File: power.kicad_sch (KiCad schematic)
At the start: 28 parts, among them J3 Conn_01x02, Q2 AO3401A, SW8 SW_Slide_DPDT, U3 TP4056-42-ESOP8, U4 INA219AxDCN, U7 TPS62160DGK

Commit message: more switch, change to sideways leds, move battery connector
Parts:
- D1: value GREEN -> ORANGE; LCSC C22371297 -> C965861; Manufacturer HONGLITRONIC -> XINGLIGHT; Manufacturer Part Number PSC-1608U52GC-G4 -> XL-1606UOC
- D2: LCSC C2286 -> C965860; Manufacturer Hubei KENTO Elec -> XINGLIGHT; Manufacturer Part Number KT-0603R -> XL-1606SURC
- D5: LCSC C22371297 -> C965863; Manufacturer HONGLITRONIC -> XINGLIGHT; Manufacturer Part Number PSC-1608U52GC-G4 -> XL-1606UGC
- SW8: footprint Button_Switch_SMD:SW_DPDT_CK_JS202011JCQN -> Button_Switch_SMD:SW_SPDT_CK_JS102011SAQN; symbol Switch:SW_Slide_DPDT -> Switch:SW_SPDT; LCSC C221665 -> C221660; Manufacturer Part Number JS202011JCQN -> JS102011SAQN
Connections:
- net at SW8.1 (A): now also R35.1, U4.1 (IN+)
- net at SW8.2 (B): now also D3.1 (K), Q2.2 (S)
- no-connect marks 4 -> 1
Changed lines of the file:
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@@
 (kicad_sch
-	(version 20260101)
+	(version 20260306)
 	(generator "eeschema")
 	(generator_version "10.0")
@@
 	)
 	(no_connect
-		(at 154.94 104.14)
-	)
-	(no_connect
-		(at 165.1 93.98)
-	)
-	(no_connect
-		(at 160.02 104.14)
-	)
-	(no_connect
-		(at 165.1 104.14)
+		(at 160.02 92.71)
 	)
 	(wire
@@
 	(wire
 		(pts
-			(xy 154.94 90.17) (xy 154.94 93.98)
-		)
-		(stroke
-			(width 0)
-			(type default)
-		)
-	)
-	(wire
-		(pts
 			(xy 226.06 57.15) (xy 246.38 57.15)
 		)
@@
 	(wire
 		(pts
+			(xy 160.02 87.63) (xy 160.02 40.64)
+		)
+		(stroke
+			(width 0)
+			(type default)
+		)
+	)
+	(wire
+		(pts
 			(xy 210.82 95.25) (xy 210.82 111.76)
 		)
@@
 	(wire
 		(pts
-			(xy 160.02 93.98) (xy 160.02 40.64)
-		)
-		(stroke
-			(width 0)
-			(type default)
-		)
-	)
-	(wire
-		(pts
 			(xy 243.84 90.17) (xy 243.84 96.52)
 		)
@@
 	(wire
 		(pts
-			(xy 143.51 90.17) (xy 154.94 90.17)
+			(xy 143.51 90.17) (xy 149.86 90.17)
 		)
 		(stroke
@@
 	)
 	(symbol
-		(lib_id "Switch:SW_Slide_DPDT")
-		(at 160.02 99.06 270)
-		(mirror x)
+		(lib_id "Switch:SW_SPDT")
+		(at 154.94 90.17 0)
 		(unit 1)
 		(body_style 1)
@@
 		(dnp no)
 		(property "Reference" "SW8"
-			(at 160.274 109.474 90)
+			(at 155.194 98.298 0)
 			(show_name no)
 			(do_not_autoplace no)
@@
 		)
 		(property "Value" "SW_Slide_DPDT"
-			(at 160.274 106.934 90)
+			(at 155.448 96.52 0)
 			(show_name no)
 			(do_not_autoplace no)
@@
 			)
 		)
-		(property "Footprint" "Button_Switch_SMD:SW_DPDT_CK_JS202011JCQN"
-			(at 165.1 85.09 0)
+		(property "Footprint" "Button_Switch_SMD:SW_SPDT_CK_JS102011SAQN"
+			(at 154.94 90.17 0)
 			(hide yes)
 			(show_name no)
@@
 		)
 		(property "Datasheet" ""
-			(at 160.02 99.06 0)
+			(at 154.94 97.79 0)
 			(hide yes)
 			(show_name no)
@@
 			)
 		)
-		(property "Description" "Slide Switch, dual pole double throw"
-			(at 160.02 99.06 0)
+		(property "Description" "Switch, single pole double throw"
+			(at 154.94 90.17 0)
 			(hide yes)
 			(show_name no)
@@
 			)
 		)
-		(property "LCSC" "C221665"
-			(at 160.02 99.06 0)
+		(property "LCSC" "C221660"
+			(at 154.94 90.17 0)
 			(hide yes)
 			(show_name no)
@@
 		)
 		(property "Manufacturer" "C&K"
-			(at 160.02 99.06 0)
+			(at 154.94 90.17 0)
 			(hide yes)
 			(show_name no)
@@
 			)
 		)
-		(property "Manufacturer Part Number" "JS202011JCQN"
-			(at 160.02 99.06 0)
+		(property "Manufacturer Part Number" "JS102011SAQN"
+			(at 154.94 90.17 0)
 			(hide yes)
 			(show_name no)
@@
 		(pin "3"
 		)
-		(pin "6"
-		)
-		(pin "4"
-		)
 		(pin "1"
 		)
 		(pin "2"
 		)
-		(pin "5"
-		)
 		(instances
 			(project "gameboy"
@@
 			)
 		)
-		(property "Description" "Light emitting diode"
+		(property "Description" "Side View Mount Light emitting diode"
 			(at 267.97 96.52 0)
 			(hide yes)
@@
 			)
 		)
-		(property "LCSC" "C22371297"
+		(property "LCSC" "C965863"
 			(at 267.97 96.52 0)
 			(hide yes)
@@
 			)
 		)
-		(property "Manufacturer" "HONGLITRONIC"
+		(property "Manufacturer" "XINGLIGHT"
 			(at 267.97 96.52 0)
 			(hide yes)
@@
 			)
 		)
-		(property "Manufacturer Part Number" "PSC-1608U52GC-G4"
+		(property "Manufacturer Part Number" "XL-1606UGC"
 			(at 267.97 96.52 0)
 			(hide yes)
@@
 			)
 		)
-		(property "Value" "GREEN"
+		(property "Value" "ORANGE"
 			(at 57.15 85.344 90)
 			(show_name no)
@@
 			)
 		)
-		(property "Description" "Light emitting diode"
+		(property "Description" "Side View Mount Light emitting diode"
 			(at 64.77 82.55 0)
 			(hide yes)
@@
 			)
 		)
-		(property "LCSC" "C22371297"
+		(property "LCSC" "C965861"
 			(at 64.77 82.55 0)
 			(hide yes)
@@
 			)
 		)
-		(property "Manufacturer" "HONGLITRONIC"
+		(property "Manufacturer" "XINGLIGHT"
 			(at 64.77 82.55 0)
 			(hide yes)
@@
 			)
 		)
-		(property "Manufacturer Part Number" "PSC-1608U52GC-G4"
+		(property "Manufacturer Part Number" "XL-1606UOC"
 			(at 64.77 82.55 0)
 			(hide yes)
@@
 			)
 		)
-		(property "Description" "Light emitting diode"
+		(property "Description" "Side View Mount Light emitting diode"
 			(at 69.85 82.55 0)
 			(hide yes)
@@
 			)
 		)
-		(property "LCSC" "C2286"
+		(property "LCSC" "C965860"
 			(at 69.85 82.55 0)
 			(hide yes)
@@
 			)
 		)
-		(property "Manufacturer" "Hubei KENTO Elec"
+		(property "Manufacturer" "XINGLIGHT"
 			(at 69.85 82.55 0)
 			(hide yes)
@@
 			)
 		)
-		(property "Manufacturer Part Number" "KT-0603R"
+		(property "Manufacturer Part Number" "XL-1606SURC"
 			(at 69.85 82.55 0)
 			(hide yes)

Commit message: custom sideways led footprint
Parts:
- D1, D2, D5: footprint LED_SMD:LED_0603_1608Metric -> RP2350_60QFN_minimal:LED_Sideways
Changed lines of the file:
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@@
 			)
 		)
-		(property "Footprint" "LED_SMD:LED_0603_1608Metric"
+		(property "Footprint" "RP2350_60QFN_minimal:LED_Sideways"
 			(at 267.97 96.52 0)
 			(hide yes)
@@
 			)
 		)
-		(property "Footprint" "LED_SMD:LED_0603_1608Metric"
+		(property "Footprint" "RP2350_60QFN_minimal:LED_Sideways"
 			(at 64.77 82.55 0)
 			(hide yes)
@@
 			)
 		)
-		(property "Footprint" "LED_SMD:LED_0603_1608Metric"
+		(property "Footprint" "RP2350_60QFN_minimal:LED_Sideways"
 			(at 69.85 82.55 0)
 			(hide yes)

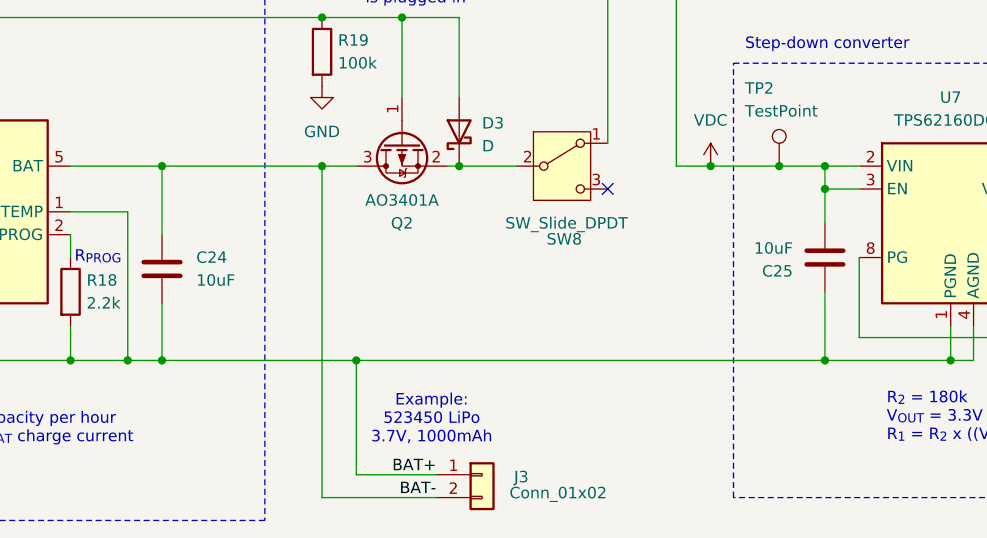
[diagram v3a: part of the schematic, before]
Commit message: changed amp sd_mode resistor value, move caps, add i2c pullups
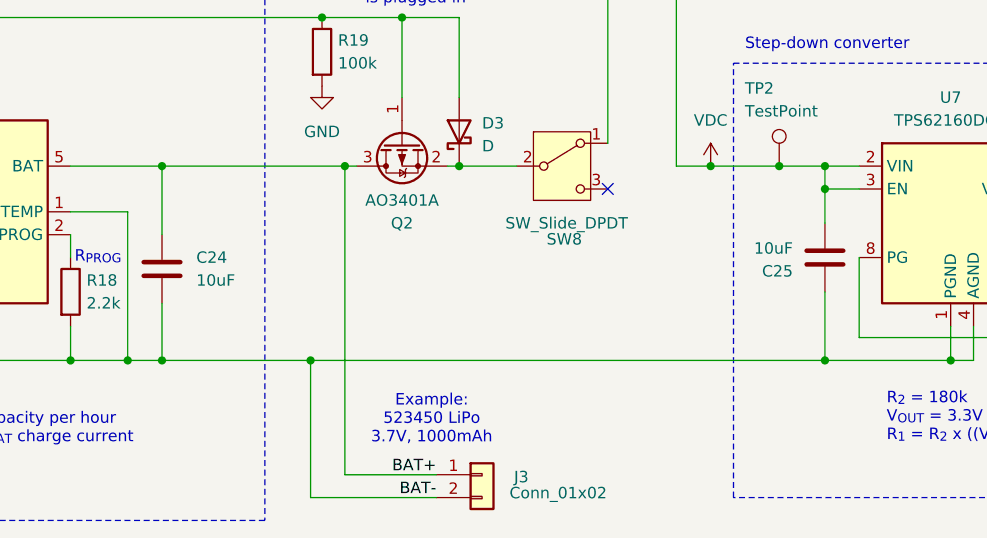
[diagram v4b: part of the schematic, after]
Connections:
- net GND: now also J3.2 (Pin_2); no longer J3.1 (Pin_1)
- net BAT- renamed BAT+
- net BAT+: now also J3.1 (Pin_1); no longer J3.2 (Pin_2)
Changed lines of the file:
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@@
-	)
-	(junction
-		(at 132.08 111.76)
-		(diameter 0)
-		(color 0 0 0 0)
 	)
 	(junction
@@
 	)
 	(junction
+		(at 130.81 90.17)
+		(diameter 0)
+		(color 0 0 0 0)
+	)
+	(junction
 		(at 184.15 90.17)
 		(diameter 0)
@@
 	)
 	(junction
+		(at 127 111.76)
+		(diameter 0)
+		(color 0 0 0 0)
+	)
+	(junction
 		(at 110.49 111.76)
 		(diameter 0)
@@
 	(junction
 		(at 267.97 90.17)
-		(diameter 0)
-		(color 0 0 0 0)
-	)
-	(junction
-		(at 128.27 90.17)
 		(diameter 0)
 		(color 0 0 0 0)
@@
 	(wire
 		(pts
-			(xy 128.27 90.17) (xy 128.27 127)
-		)
-		(stroke
-			(width 0)
-			(type default)
-		)
-	)
-	(wire
-		(pts
 			(xy 64.77 93.98) (xy 64.77 97.79)
 		)
@@
 	(wire
 		(pts
-			(xy 132.08 111.76) (xy 184.15 111.76)
-		)
-		(stroke
-			(width 0)
-			(type default)
-		)
-	)
-	(wire
-		(pts
 			(xy 143.51 73.66) (xy 143.51 82.55)
 		)
@@
 	(wire
 		(pts
-			(xy 128.27 127) (xy 140.97 127)
-		)
-		(stroke
-			(width 0)
-			(type default)
-		)
-	)
-	(wire
-		(pts
 			(xy 87.63 107.95) (xy 87.63 111.76)
 		)
@@
 	(wire
 		(pts
-			(xy 132.08 124.46) (xy 140.97 124.46)
-		)
-		(stroke
-			(width 0)
-			(type default)
-		)
-	)
-	(wire
-		(pts
 			(xy 80.01 73.66) (xy 90.17 73.66)
 		)
@@
 	(wire
 		(pts
+			(xy 130.81 124.46) (xy 140.97 124.46)
+		)
+		(stroke
+			(width 0)
+			(type default)
+		)
+	)
+	(wire
+		(pts
 			(xy 226.06 57.15) (xy 246.38 57.15)
 		)
@@
 	(wire
 		(pts
-			(xy 110.49 111.76) (xy 132.08 111.76)
+			(xy 110.49 111.76) (xy 127 111.76)
 		)
 		(stroke
@@
 	(wire
 		(pts
+			(xy 127 127) (xy 140.97 127)
+		)
+		(stroke
+			(width 0)
+			(type default)
+		)
+	)
+	(wire
+		(pts
 			(xy 224.79 49.53) (xy 226.06 49.53)
 		)
@@
 	(wire
 		(pts
-			(xy 128.27 90.17) (xy 132.08 90.17)
+			(xy 110.49 90.17) (xy 130.81 90.17)
 		)
 		(stroke
@@
 	(wire
 		(pts
+			(xy 130.81 124.46) (xy 130.81 90.17)
+		)
+		(stroke
+			(width 0)
+			(type default)
+		)
+	)
+	(wire
+		(pts
 			(xy 209.55 90.17) (xy 208.28 90.17)
 		)
@@
 	(wire
 		(pts
-			(xy 132.08 111.76) (xy 132.08 124.46)
+			(xy 127 127) (xy 127 111.76)
 		)
 		(stroke
@@
 	(wire
 		(pts
+			(xy 130.81 90.17) (xy 132.08 90.17)
+		)
+		(stroke
+			(width 0)
+			(type default)
+		)
+	)
+	(wire
+		(pts
 			(xy 184.15 90.17) (xy 187.96 90.17)
 		)
@@
 	(wire
 		(pts
+			(xy 127 111.76) (xy 184.15 111.76)
+		)
+		(stroke
+			(width 0)
+			(type default)
+		)
+	)
+	(wire
+		(pts
 			(xy 69.85 73.66) (xy 80.01 73.66)
 		)
@@
 		)
 		(stroke
-			(width 0)
-			(type default)
-		)
-	)
-	(wire
-		(pts
-			(xy 110.49 90.17) (xy 128.27 90.17)
-		)
-		(stroke

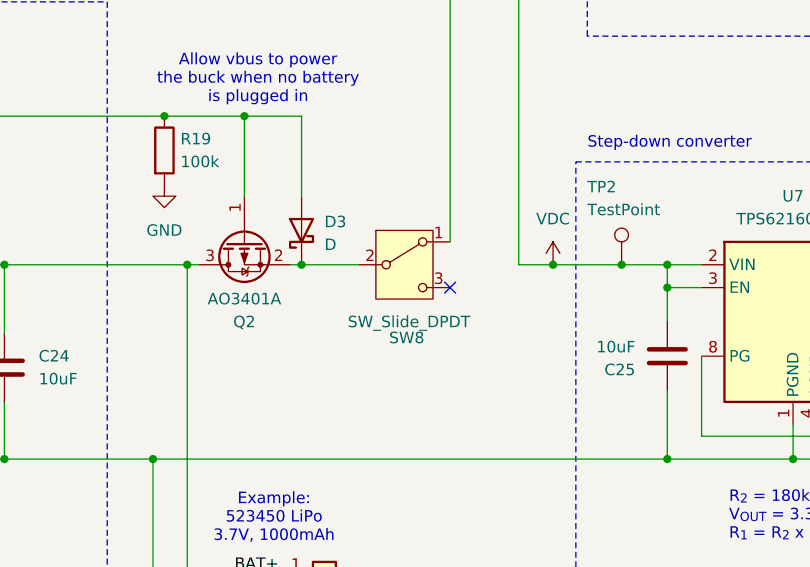
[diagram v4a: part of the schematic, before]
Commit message: update components
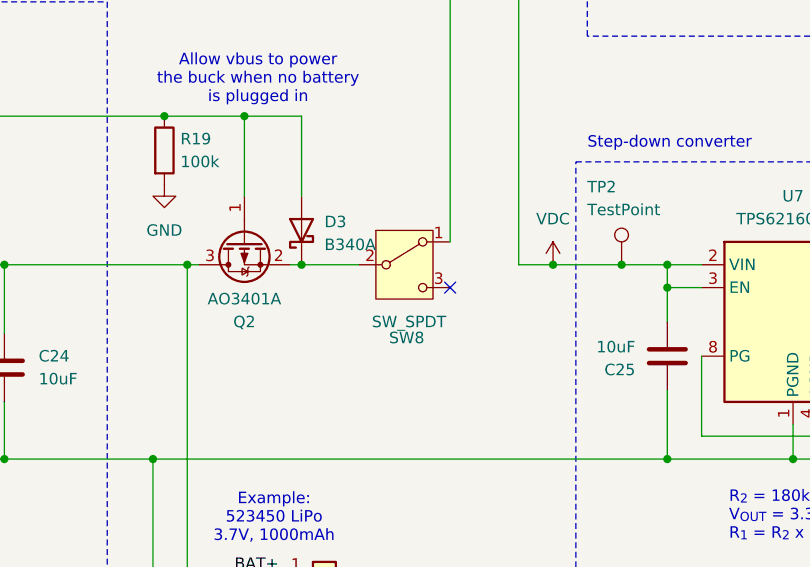
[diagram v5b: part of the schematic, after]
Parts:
- C32: LCSC (none) -> C52923; Manufacturer (none) -> Samsung Electro-Mechanics; Manufacturer Part Number (none) -> CL05A105KA5NQNC
- D3: value D -> B340A
- D5: LCSC C965863 -> C965864; Manufacturer Part Number XL-1606UGC -> XL-1606SYGC
- SW8: value SW_Slide_DPDT -> SW_SPDT
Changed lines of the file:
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@@
 			)
 		)
-		(property "Value" "SW_Slide_DPDT"
+		(property "Value" "SW_SPDT"
 			(at 155.448 96.52 0)
 			(show_name no)
@@
 			)
 		)
-		(property "LCSC" "C965863"
+		(property "LCSC" "C965864"
 			(at 267.97 96.52 0)
 			(hide yes)
@@
 			)
 		)
-		(property "Manufacturer Part Number" "XL-1606UGC"
+		(property "Manufacturer Part Number" "XL-1606SYGC"
 			(at 267.97 96.52 0)
 			(hide yes)
@@
 			)
 		)
-		(property "LCSC" ""
+		(property "LCSC" "C52923"
 			(at 246.38 43.18 0)
 			(hide yes)
@@
 			)
 		)
-	)
+		(property "Manufacturer" "Samsung Electro-Mechanics"
+			(at 246.38 43.18 0)
+			(hide yes)
+			(effects
+				(font
+					(size 1.27 1.27)
+				)
+			)
+		)
+		(property "Manufacturer Part Number" "CL05A105KA5NQNC"
+			(at 246.38 43.18 0)
+			(hide yes)
+			(effects
+				(font
+					(size 1.27 1.27)
+				)
+			)
+		))
 	(symbol
 		(lib_id "Device:D_Schottky")
@@
 			)
 		)
-		(property "Value" "D"
+		(property "Value" "B340A"
 			(at 146.05 87.9474 90)
 			(show_name no)
